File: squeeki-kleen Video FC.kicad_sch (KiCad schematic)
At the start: 11 parts, among them J1 VCC, J2 VOUT, J3 GND, J4 CVBS, J5 GND, Q1 MMBT3906

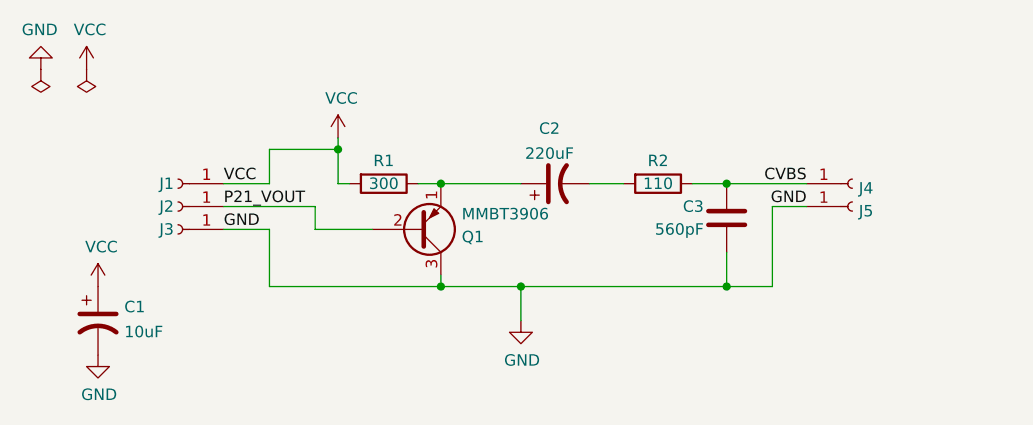
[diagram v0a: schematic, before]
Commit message: Big changes
- Fix MMBT3906 pinout
- Use NPTH instead of edge cut circles
- Update silkscreen art
- Add 100uF electrolytic capacitor for power
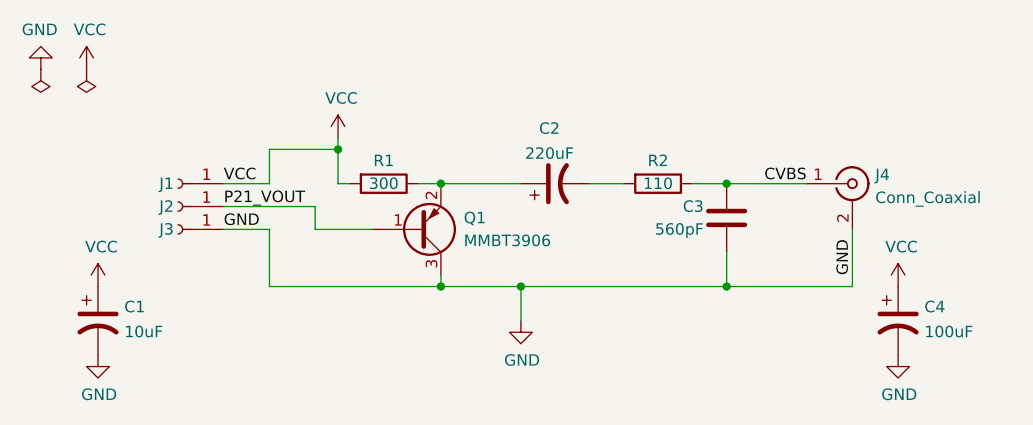
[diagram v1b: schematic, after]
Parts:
- removed J4: CVBS, custom footprints:Pad_SMD_3.81x1.27mm, symbol Connector:Conn_01x01_Female
- removed J5: GND, custom footprints:Pad_SMD_3.81x1.27mm, symbol Connector:Conn_01x01_Female
- removed Q1: MMBT3906, Package_TO_SOT_SMD:SOT-23, symbol Transistor_BJT:2N3906
- added C4: 100uF, Capacitor_SMD:CP_Elec_6.3x4.5, symbol Device:C_Polarized_US
- added J4: Conn_Coaxial, Connector_Coaxial:MMCX_Molex_73415-0961_Horizontal_0.8mm-PCB, symbol Connector:Conn_Coaxial
- added Q1: MMBT3906, Package_TO_SOT_SMD:SOT-23, symbol Device:Q_PNP_BEC
- C2: footprint Capacitor_SMD:C_Elec_6.3x5.4 -> Capacitor_SMD:CP_Elec_6.3x5.4
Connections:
- net CVBS: now also J4.1 (In)
- net GND: now also C4.2, J4.2 (Ext), Q1.3 (C)
- net P21_VOUT: now also Q1.1 (B)
- net VCC: now also C4.1
- net at C2.1, R1.1: now also Q1.2 (E)
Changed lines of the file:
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@@
   (junction (at 59.69 31.75) (diameter 0) (color 0 0 0 0)
   )
-  (wire (pts (xy 96.52 34.29) (xy 96.52 43.18))
+  (wire (pts (xy 59.69 31.75) (xy 68.58 31.75))
     (stroke (width 0) (type default) (color 0 0 0 0))
   )
@@
     (stroke (width 0) (type default) (color 0 0 0 0))
   )
-  (wire (pts (xy 91.44 43.18) (xy 96.52 43.18))
-    (stroke (width 0) (type default) (color 0 0 0 0))
-  )
   (wire (pts (xy 40.64 27.94) (xy 48.26 27.94))
     (stroke (width 0) (type default) (color 0 0 0 0))
@@
     (stroke (width 0) (type default) (color 0 0 0 0))
   )
+  (wire (pts (xy 91.44 43.18) (xy 105.41 43.18))
+    (stroke (width 0) (type default) (color 0 0 0 0))
+  )
   (wire (pts (xy 91.44 31.75) (xy 100.33 31.75))
     (stroke (width 0) (type default) (color 0 0 0 0))
@@
     (stroke (width 0) (type default) (color 0 0 0 0))
   )
-  (wire (pts (xy 68.58 31.75) (xy 59.69 31.75))
-    (stroke (width 0) (type default) (color 0 0 0 0))
-  )
   (wire (pts (xy 68.58 43.18) (xy 68.58 46.99))
     (stroke (width 0) (type default) (color 0 0 0 0))
   )
-  (wire (pts (xy 96.52 34.29) (xy 100.33 34.29))
+  (wire (pts (xy 105.41 43.18) (xy 105.41 36.83))
     (stroke (width 0) (type default) (color 0 0 0 0))
   )
@@
     (effects (font (size 1.27 1.27)) (justify left bottom))
   )
-  (label "GND" (at 100.33 34.29 180)
-    (effects (font (size 1.27 1.27)) (justify right bottom))
+  (label "GND" (at 105.41 41.91 90)
+    (effects (font (size 1.27 1.27)) (justify left bottom))
   )
   (symbol (lib_id "Connector:Conn_01x01_Female") (at 30.48 36.83 180) (unit 1)
@@
     )
     (property "Datasheet" "~" (id 3) (at 30.48 34.29 0)
-      (effects (font (size 1.27 1.27)) hide)
-    )
-    (pin "1")
-  )
-  (symbol (lib_id "Connector:Conn_01x01_Female") (at 105.41 31.75 0) (unit 1)
-    (in_bom yes) (on_board yes)
-    (property "Reference" "J4" (id 0) (at 106.1212 32.258 0)
-      (effects (font (size 1.27 1.27)) (justify left))
-    )
-    (property "Value" "CVBS" (id 1) (at 106.1212 33.401 0)
-      (effects (font (size 1.27 1.27)) (justify left) hide)
-    )
-    (property "Footprint" "custom footprints:Pad_SMD_3.81x1.27mm" (id 2) (at 105.41 31.75 0)
-      (effects (font (size 1.27 1.27)) hide)
-    )
-    (property "Datasheet" "~" (id 3) (at 105.41 31.75 0)
-      (effects (font (size 1.27 1.27)) hide)
-    )
-    (pin "1")
-  )
-  (symbol (lib_id "Connector:Conn_01x01_Female") (at 105.41 34.29 0) (unit 1)
-    (in_bom yes) (on_board yes)
-    (property "Reference" "J5" (id 0) (at 106.1212 34.798 0)
-      (effects (font (size 1.27 1.27)) (justify left))
-    )
-    (property "Value" "GND" (id 1) (at 106.1212 35.941 0)
-      (effects (font (size 1.27 1.27)) (justify left) hide)
-    )
-    (property "Footprint" "custom footprints:Pad_SMD_3.81x1.27mm" (id 2) (at 105.41 34.29 0)
-      (effects (font (size 1.27 1.27)) hide)
-    )
-    (property "Datasheet" "~" (id 3) (at 105.41 34.29 0)
       (effects (font (size 1.27 1.27)) hide)
     )
@@
     (pin "1")
   )
-  (symbol (lib_id "Transistor_BJT:2N3906") (at 57.15 36.83 0) (mirror x) (unit 1)
+  (symbol (lib_id "power:GND") (at 110.49 50.8 0) (unit 1)
+    (in_bom yes) (on_board yes)
+    (property "Reference" "#PWR08" (id 0) (at 110.49 57.15 0)
+      (effects (font (size 1.27 1.27)) hide)
+    )
+    (property "Value" "GND" (id 1) (at 110.617 55.1942 0))
+    (property "Footprint" "" (id 2) (at 110.49 50.8 0)
+      (effects (font (size 1.27 1.27)) hide)
+    )
+    (property "Datasheet" "" (id 3) (at 110.49 50.8 0)
+      (effects (font (size 1.27 1.27)) hide)
+    )
+    (pin "1")
+  )
+  (symbol (lib_id "Device:Q_PNP_BEC") (at 57.15 36.83 0) (mirror x) (unit 1)
     (in_bom yes) (on_board yes) (fields_autoplaced)
-    (property "Reference" "Q1" (id 0) (at 62.0014 37.6647 0)
-      (effects (font (size 1.27 1.27)) (justify left))
-    )
-    (property "Value" "MMBT3906" (id 1) (at 62.0014 35.1278 0)
-      (effects (font (size 1.27 1.27)) (justify left))
-    )
-    (property "Footprint" "Package_TO_SOT_SMD:SOT-23" (id 2) (at 62.23 34.925 0)
-      (effects (font (size 1.27 1.27) italic) (justify left) hide)
-    )
-    (property "Datasheet" "https://www.onsemi.com/pub/Collateral/2N3906-D.PDF" (id 3) (at 57.15 36.83 0)
-      (effects (font (size 1.27 1.27)) (justify left) hide)
-    )
-    (property "LCSC" "C2891809" (id 4) (at 57.15 36.83 0)
+    (property "Reference" "Q1" (id 0) (at 62.23 35.5599 0)
+      (effects (font (size 1.27 1.27)) (justify left))
+    )
+    (property "Value" "MMBT3906" (id 1) (at 62.23 38.0999 0)
+      (effects (font (size 1.27 1.27)) (justify left))
+    )
+    (property "Footprint" "Package_TO_SOT_SMD:SOT-23" (id 2) (at 62.23 39.37 0)
+      (effects (font (size 1.27 1.27)) hide)
+    )
+    (property "Datasheet" "https://datasheet.lcsc.com/lcsc/2109011130_YONGYUTAI-MMBT3906_C2891809.pdf" (id 3) (at 57.15 36.83 0)
       (effects (font (size 1.27 1.27)) hide)
     )
@@
     (property "Reference" "C2" (id 0) (at 71.755 25.6245 90))
     (property "Value" "220uF" (id 1) (at 71.755 28.3996 90))
-    (property "Footprint" "Capacitor_SMD:C_Elec_6.3x5.4" (id 2) (at 72.39 31.75 0)
+    (property "Footprint" "Capacitor_SMD:CP_Elec_6.3x5.4" (id 2) (at 72.39 31.75 0)
       (effects (font (size 1.27 1.27)) hide)
     )
@@
     (pin "1")
     (pin "2")
+  )
+  (symbol (lib_id "Connector:Conn_Coaxial") (at 105.41 31.75 0) (unit 1)
+    (in_bom yes) (on_board yes) (fields_autoplaced)
+    (property "Reference" "J4" (id 0) (at 107.95 30.7731 0)
+      (effects (font (size 1.27 1.27)) (justify left))
+    )
+    (property "Value" "Conn_Coaxial" (id 1) (at 107.95 33.3131 0)
+      (effects (font (size 1.27 1.27)) (justify left))
+    )
+    (property "Footprint" "Connector_Coaxial:MMCX_Molex_73415-0961_Horizontal_0.8mm-PCB" (id 2) (at 105.41 31.75 0)
+      (effects (font (size 1.27 1.27)) hide)
+    )
+    (property "Datasheet" " ~" (id 3) (at 105.41 31.75 0)
+      (effects (font (size 1.27 1.27)) hide)
+    )
+    (pin "1")
+    (pin "2")
+  )
+  (symbol (lib_id "Device:C_Polarized_US") (at 110.49 46.99 0) (unit 1)
+    (in_bom yes) (on_board yes) (fields_autoplaced)
+    (property "Reference" "C4" (id 0) (at 113.411 45.4465 0)
+      (effects (font (size 1.27 1.27)) (justify left))
+    )
+    (property "Value" "100uF" (id 1) (at 113.411 48.2216 0)
+      (effects (font (size 1.27 1.27)) (justify left))
+    )
+    (property "Footprint" "Capacitor_SMD:CP_Elec_6.3x4.5" (id 2) (at 110.49 46.99 0)
+      (effects (font (size 1.27 1.27)) hide)
+    )
+    (property "Datasheet" "~" (id 3) (at 110.49 46.99 0)
+      (effects (font (size 1.27 1.27)) hide)
+    )
+    (property "LCSC" "C1508940" (id 4) (at 110.49 46.99 0)
+      (effects (font (size 1.27 1.27)) hide)
+    )
+    (pin "1")
+    (pin "2")
+  )
+  (symbol (lib_id "power:VCC") (at 110.49 43.18 0) (unit 1)
+    (in_bom yes) (on_board yes)
+    (property "Reference" "#PWR07" (id 0) (at 110.49 46.99 0)
+      (effects (font (size 1.27 1.27)) hide)
+    )
+    (property "Value" "VCC" (id 1) (at 110.871 38.7858 0))
+    (property "Footprint" "" (id 2) (at 110.49 43.18 0)
+      (effects (font (size 1.27 1.27)) hide)
+    )
+    (property "Datasheet" "" (id 3) (at 110.49 43.18 0)
+      (effects (font (size 1.27 1.27)) hide)
+    )
+    (pin "1")
   )
   (symbol (lib_id "Device:C_Polarized_US") (at 21.59 46.99 0) (unit 1)
@@
       (reference "#PWR06") (unit 1) (value "GND") (footprint "")
     )
+    (path "/982eb10b-a905-4af1-b112-e13d062bf793"
+      (reference "#PWR07") (unit 1) (value "VCC") (footprint "")
+    )
+    (path "/0790faf9-639f-4440-bb04-64992bb99fbe"
+      (reference "#PWR08") (unit 1) (value "GND") (footprint "")
+    )
     (path "/b64604b9-aaa3-4f13-9f63-333ea99f4f56"
       (reference "C1") (unit 1) (value "10uF") (footprint "Capacitor_Tantalum_SMD:CP_EIA-3216-18_Kemet-A_Pad1.58x1.35mm_HandSolder")
     )
     (path "/37af7ef2-de1c-4d41-890c-7551e9dafc96"
-      (reference "C2") (unit 1) (value "220uF") (footprint "Capacitor_SMD:C_Elec_6.3x5.4")
+      (reference "C2") (unit 1) (value "220uF") (footprint "Capacitor_SMD:CP_Elec_6.3x5.4")
     )
     (path "/00000000-0000-0000-0000-0000611b09b2"
       (reference "C3") (unit 1) (value "560pF") (footprint "Capacitor_SMD:C_0805_2012Metric_Pad1.18x1.45mm_HandSolder")
     )
+    (path "/6696927c-6949-4be7-ab68-c0449406ccdd"
+      (reference "C4") (unit 1) (value "100uF") (footprint "Capacitor_SMD:CP_Elec_6.3x4.5")
+    )
     (path "/00000000-0000-0000-0000-0000611aaf0d"
       (reference "J1") (unit 1) (value "VCC") (footprint "custom footprints:THT_Hole")
@@
       (reference "J3") (unit 1) (value "GND") (footprint "custom footprints:THT_Hole")
     )
-    (path "/00000000-0000-0000-0000-0000611ab2ac"
-      (reference "J4") (unit 1) (value "CVBS") (footprint "custom footprints:Pad_SMD_3.81x1.27mm")
-    )
-    (path "/00000000-0000-0000-0000-0000611abcc1"
-      (reference "J5") (unit 1) (value "GND") (footprint "custom footprints:Pad_SMD_3.81x1.27mm")
-    )
-    (path "/16120871-e072-47f7-bc6e-6f3851d08cce"
+    (path "/54b2f989-1743-4edb-95c0-36aa66c82c4d"
+      (reference "J4") (unit 1) (value "Conn_Coaxial") (footprint "Connector_Coaxial:MMCX_Molex_73415-0961_Horizontal_0.8mm-PCB")
+    )
+    (path "/26b9d794-5ea5-421c-b1bd-6e3e2ca52f32"
       (reference "Q1") (unit 1) (value "MMBT3906") (footprint "Package_TO_SOT_SMD:SOT-23")
     )
